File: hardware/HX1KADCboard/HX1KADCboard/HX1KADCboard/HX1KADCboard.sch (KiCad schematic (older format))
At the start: 36 parts, among them J1 Conn_02x05_Odd_Even, J2 Conn_01x20_Male, J3 Conn_01x20_Male, J4 Conn_01x20_Male, J5 Conn_01x20_Male, J6 Conn_01x03_Male, U1 LTC3406ES5, U2 AT25SF081-SSHD-X, U3 ICE40HX1K-VQ100(VQFP100)

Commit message: ice40HX1K + SRAM board
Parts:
- removed J3, J4: Conn_01x20_Male, Connector_PinHeader_2.54mm:PinHeader_1x20_P2.54mm_Vertical, symbol Connector:Conn_01x20_Male
- removed U3: ICE40HX1K-VQ100(VQFP100), Package_QFP:LQFP-100_14x14mm_P0.5mm, symbol ice40HX1Kboard-rescue:ICE40HX1K-VQ100(VQFP100)-kilib
- added C18, C19: 0.1uF, Capacitor_SMD:C_0805_2012Metric, symbol Device:C
- added D2, D3, D4, D5: LED, LED_SMD:LED_1206_3216Metric, symbol Device:LED
- added R10, R11, R12, R9: 10kohm, Resistor_SMD:R_1206_3216Metric, symbol Device:R
- added U3: ICE40HX1K-VQ100(VQFP100), Package_QFP:LQFP-100_14x14mm_P0.5mm, symbol kilib:ICE40HX1K-VQ100(VQFP100)
- added U4: AS7C34096A, Package_SO:TSOP-II-44_10.16x18.41mm_P0.8mm, symbol kilib:AS7C34096A
- C1: value C -> 4.7uF
- C3: value C -> 10uF
- L1: value L -> 2.2uH
- R7, R8: value R -> 100kOhm
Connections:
- net +1V2: now also U3.11 (VCC), U3.35 (VCC), U3.61 (VCC), U3.77 (VCC)
- net +3V3: now also C18.2, C19.2, U3.14 (VCCIO_3), U3.22 (VCCIO_3), U3.31 (VCCIO_2), U3.38 (VCCIO_2), U3.50 (VCC_SPI), U3.58 (VCCIO_1), U3.6 (VCCIO_3), U3.67 (VCCIO_1), U3.88 (VCCIO_0), U3.92 (VCCIO_0), U4.11 (Vcc), U4.33 (Vcc)
- net CDONE: now also D2.2 (A), U3.43 (CDONE)
- net CRESET: now also U3.44 (CRESET_B)
- net GND: now also C18.1, C19.1, R10.1, R11.1, R12.1, R9.1, U3.17 (GND), U3.23 (GND), U3.32 (GND), U3.39 (GND), U3.47 (GND), U3.5 (GND), U3.55 (GND), U3.70 (GND), U3.84 (GND), U3.98 (GND), U4.12 (GND), U4.34 (GND)
- net IO1: now also U3.1 (IOL_1A), U4.27 (A11)
- net IO10: now also U3.10 (IOL_5B), U4.15 (WE#)
- net IO100: now also U3.100 (IOT_95)
- net IO12: now also U3.12 (IOL_6A), U4.14 (D4)
- net IO13: now also U3.13 (IOL_6B_GBIN7), U4.13 (D3)
- net IO15: now also U3.15 (IOL_7A_GBIN6), U4.10 (D2)
- net IO16: now also U3.16 (IOL_7B), U4.9 (D1)
- net IO18: now also U3.18 (IOL_8A), U4.8 (CE#)
- net IO19: now also U3.19 (IOL_8B), U4.7 (A4)
- net IO2: now also U3.2 (IOL_1B), U4.26 (A10)
- net IO20: now also U3.20 (IOL_10A), U4.6 (A3)
- net IO21: now also U3.21 (IOL_10B), U4.5 (A2)
- net IO24: now also U3.24 (IOL_12A), U4.4 (A1)
- net IO25: now also U3.25 (IOL_12B), U4.3 (A0)
- net IO26: now also U3.26 (IOB_26), U4.41 (A18)
- net IO27: now also U3.27 (IOB_27), U4.40 (A17)
- net IO28: now also U3.28 (IOB_28), U4.39 (A16)
- net IO29: now also U3.29 (IOB_29), U4.38 (A15)
- net IO3: now also U3.3 (IOL_2A), U4.20 (A9)
- net IO30: now also U3.30 (IOB_30), U4.37 (OE#)
- net IO33: now also U3.33 (IOB_35_GBIN5), U4.36 (D8)
- net IO34: now also U3.34 (IOB_36_GBIN4), U4.35 (D7)
- net IO36: now also U3.36 (IOB_34), U4.32 (D6)
- net IO37: now also U3.37 (IOB_37), U4.31 (D5)
- net IO4: now also U3.4 (IOL_2B), U4.19 (A8)
- net IO40: now also U3.40 (IOB_41), U4.30 (A14)
- net IO41: now also U3.41 (IOB_42_CBSEL0), U4.29 (A13)
- net IO43: now also U3.42 (IOB_43_CBSEL1), U4.28 (A12)
- net IO51: now also D5.2 (A), U3.51 (IOR_52)
- net IO52: now also D4.2 (A), U3.52 (IOR_53)
- net IO53: now also D3.2 (A), U3.53 (IOR_54)
- net IO54: now also U3.54 (IOR_55)
- net IO56: now also U3.56 (IOR_56)
- net IO57: now also U3.57 (IOR_57)
- net IO59: now also U3.59 (IOR_58)
- net IO60: now also U3.60 (IOR_59)
- net IO62: now also U3.62 (IOR_60_GBIN3)
- net IO63: now also U3.63 (IOR_61_GBIN2)
- net IO64: now also U3.64 (IOR_63)
- net IO65: now also U3.65 (IOR_64)
- net IO66: now also U3.66 (IOR_65)
- net IO68: now also U3.68 (IOR_67)
- net IO69: now also U3.69 (IOR_68)
- net IO7: now also U3.7 (IOL_3A), U4.18 (A7)
- net IO71: now also U3.71 (IOR_69)
- net IO72: now also U3.72 (IOR_70)
- net IO73: now also U3.73 (IOR_71)
- net IO74: now also U3.74 (IOR_72)
- net IO78: now also U3.78 (IOT_73)
- net IO79: now also U3.79 (IOT_74)
- net IO8: now also U3.8 (IOL_3B), U4.17 (A6)
- net IO80: now also U3.80 (IOT_75)
- net IO81: now also U3.81 (IOT_77)
- net IO82: now also U3.82 (IOT_78)
- net IO83: now also U3.83 (IOT_79)
- net IO85: now also U3.85 (IOT_80)
- net IO86: now also U3.86 (IOT_81)
- net IO87: now also U3.87 (IOT_82)
- net IO89: now also U3.89 (IOT_84_GBIN1)
- net IO9: now also U3.9 (IOL_5A), U4.16 (A5)
- net IO90: now also U3.90 (IOT_85_GBIN0)
- net IO91: now also U3.91 (IOT_86)
- net IO93: now also U3.93 (IOT_87)
- net IO94: now also U3.94 (IOT_88)
- net IO95: now also U3.95 (IOT_89)
- net IO96: now also U3.96 (IOT_90)
- net IO97: now also U3.97 (IOT_91)
- net IO99: now also U3.99 (IOT_93)
- net SPI_CS: now also U3.49 (IOB_47_SS)
- net SPI_IN: now also U3.46 (IOB_45_SDI)
- net SPI_OUT: now also U3.45 (IOB_44_SDO)
- net SPI_SCK: now also U3.48 (IOB_46_SCK)
- net at D1.1 (K): now also U3.75 (VPP_2V5)
- new net: D2.1 (K), R9.2
- new net: D3.1 (K), R10.2
- new net: D4.1 (K), R11.2
- new net: D5.1 (K), R12.2

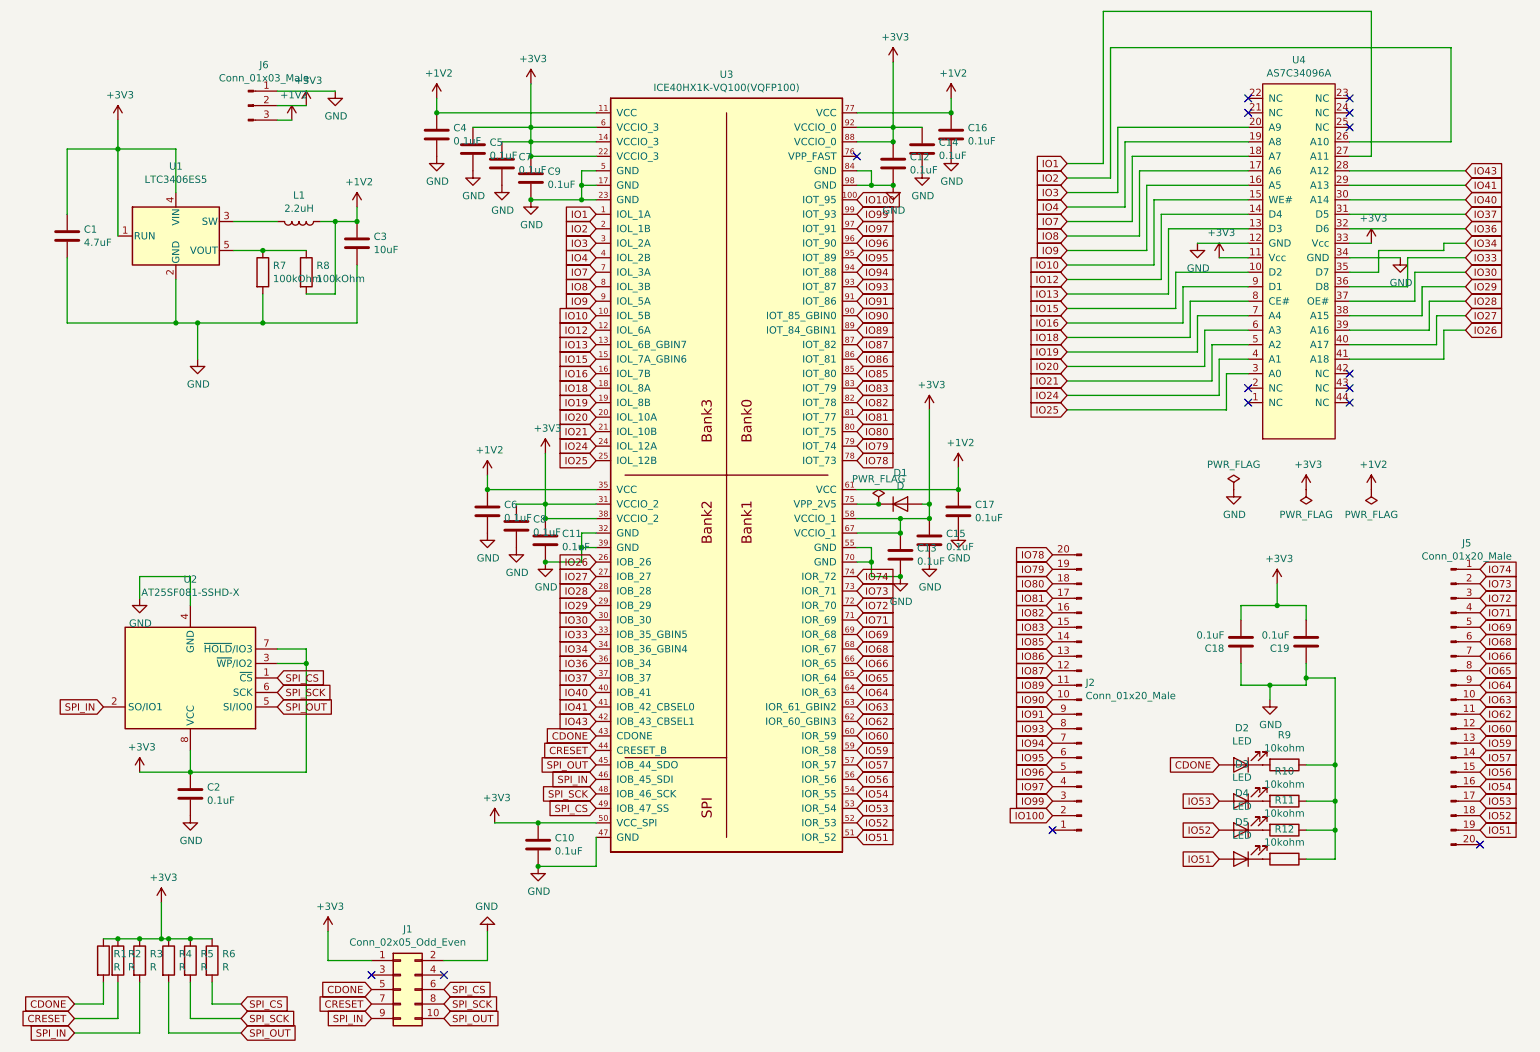
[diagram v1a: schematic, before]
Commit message: new ice40HX1K SRAM board
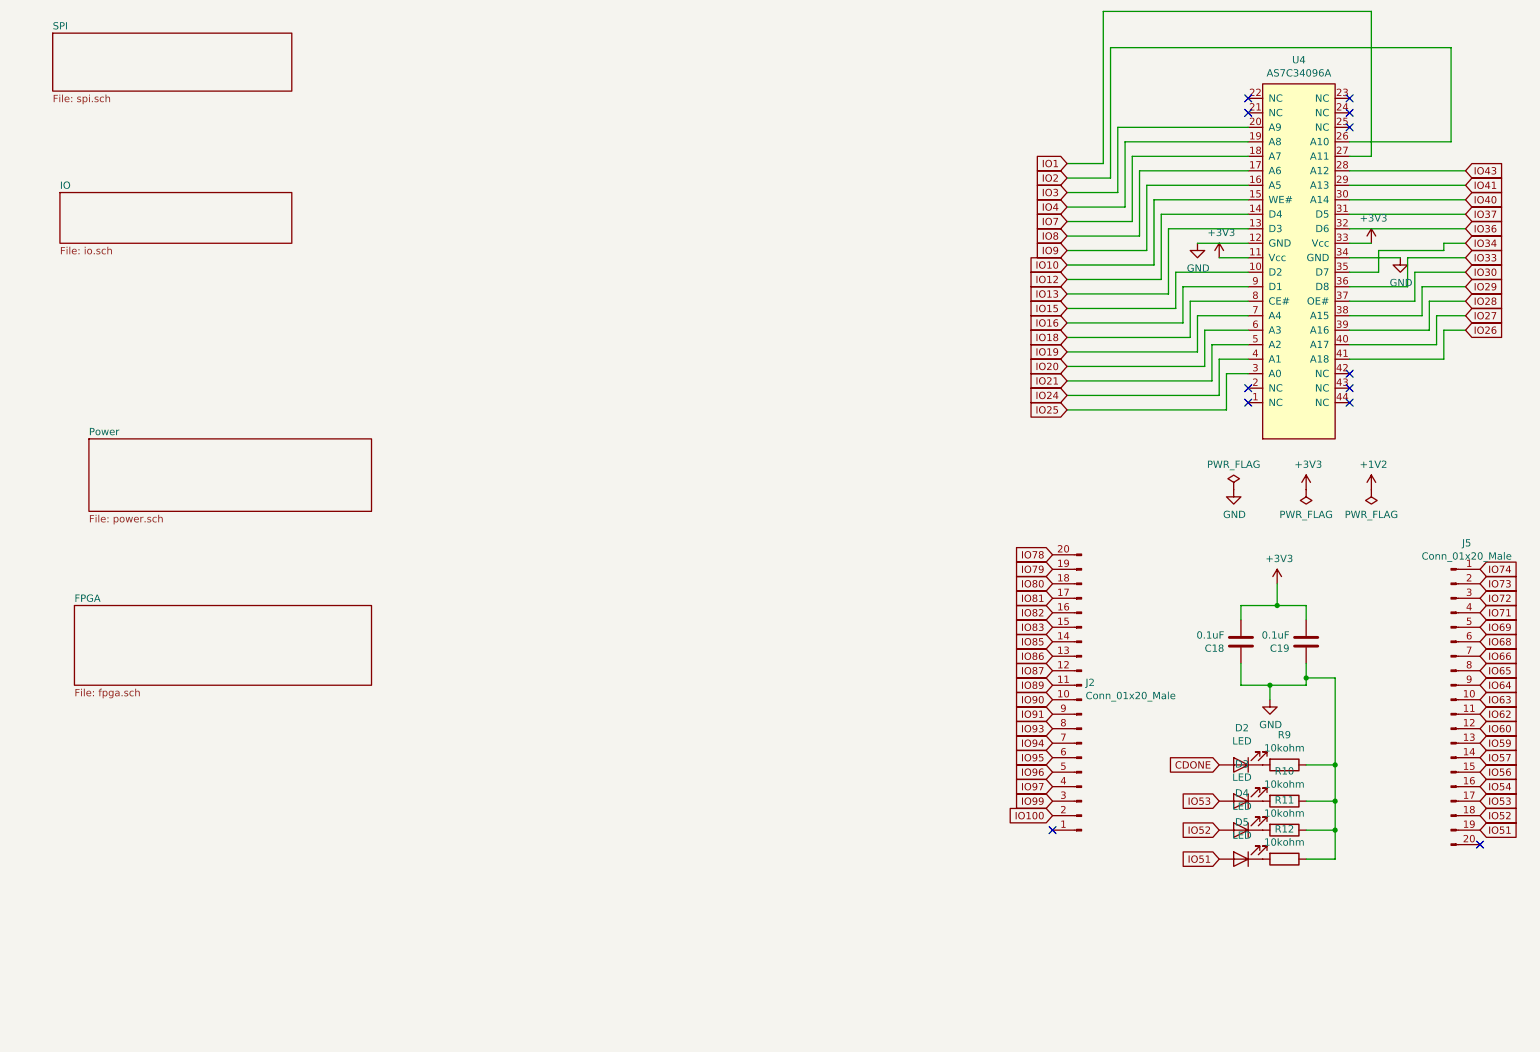
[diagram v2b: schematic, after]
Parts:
- removed C1: 4.7uF, Capacitor_SMD:C_1206_3216Metric, symbol Device:C
- removed C10, C11, C12, C13, C14, C15, C16, C17, C2, C4, C5, C6, C7, C8, C9: 0.1uF, Capacitor_SMD:C_0805_2012Metric, symbol Device:C
- removed C3: 10uF, Capacitor_SMD:C_1206_3216Metric, symbol Device:C
- removed D1: D, Capacitor_SMD:C_0603_1608Metric, symbol Device:D
- removed J1: Conn_02x05_Odd_Even, Connector_PinHeader_2.54mm:PinHeader_2x05_P2.54mm_Vertical, symbol Connector_Generic:Conn_02x05_Odd_Even
- removed J6: Conn_01x03_Male, Connector_PinHeader_2.54mm:PinHeader_1x03_P2.54mm_Vertical, symbol Connector:Conn_01x03_Male
- removed L1: 2.2uH, Inductor_SMD:L_1210_3225Metric, symbol Device:L
- removed R1, R2, R3, R4, R5, R6: R, Resistor_SMD:R_1206_3216Metric, symbol Device:R
- removed R7, R8: 100kOhm, Resistor_SMD:R_1206_3216Metric, symbol Device:R
- removed U1: LTC3406ES5, Package_TO_SOT_SMD:TSOT-23-5, symbol Regulator_Switching:LTC3406ES5
- removed U2: AT25SF081-SSHD-X, Package_SO:SOIC-8_3.9x4.9mm_P1.27mm, symbol Memory_Flash:AT25SF081-SSHD-X
- removed U3: ICE40HX1K-VQ100(VQFP100), Package_QFP:LQFP-100_14x14mm_P0.5mm, symbol kilib:ICE40HX1K-VQ100(VQFP100)
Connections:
- no-connect marks 15 -> 12

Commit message: ice40HX1K board next with SRAM AS7C34096A
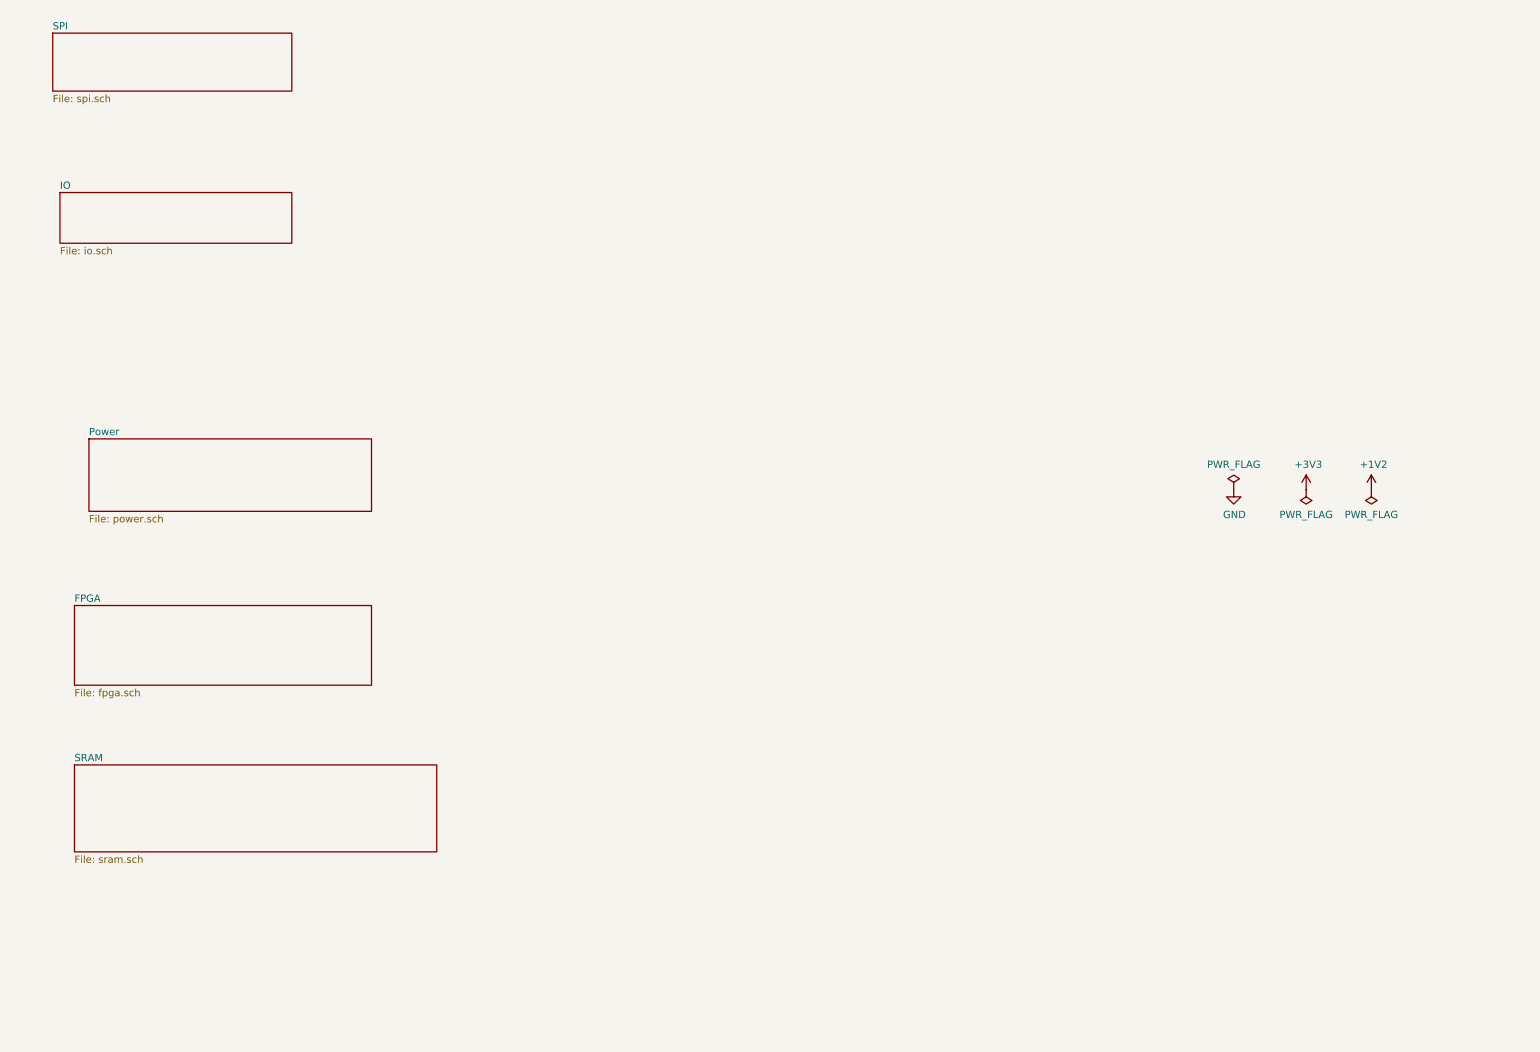
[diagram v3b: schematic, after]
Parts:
- removed C18, C19: 0.1uF, Capacitor_SMD:C_0805_2012Metric, symbol Device:C
- removed D2, D3, D4, D5: LED, LED_SMD:LED_1206_3216Metric, symbol Device:LED
- removed J2, J5: Conn_01x20_Male, Connector_PinHeader_2.54mm:PinHeader_1x20_P2.54mm_Vertical, symbol Connector:Conn_01x20_Male
- removed R10, R11, R12, R9: 10kohm, Resistor_SMD:R_1206_3216Metric, symbol Device:R
- removed U4: AS7C34096A, Package_SO:TSOP-II-44_10.16x18.41mm_P0.8mm, symbol kilib:AS7C34096A
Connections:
- no-connect marks 12 -> 0
